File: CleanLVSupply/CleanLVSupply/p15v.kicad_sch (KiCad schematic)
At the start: 19 parts, among them U3 LMR64010XMF, U4 TPS7A47

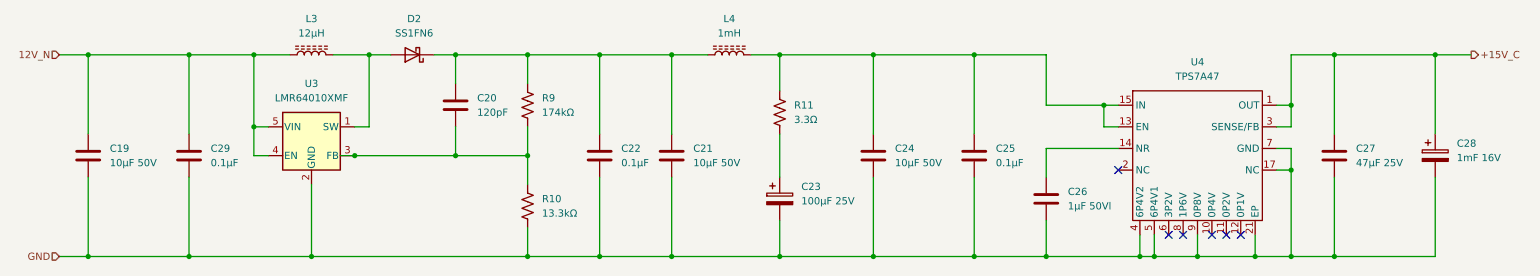
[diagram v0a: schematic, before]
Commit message: CleanLVSupply routing progress
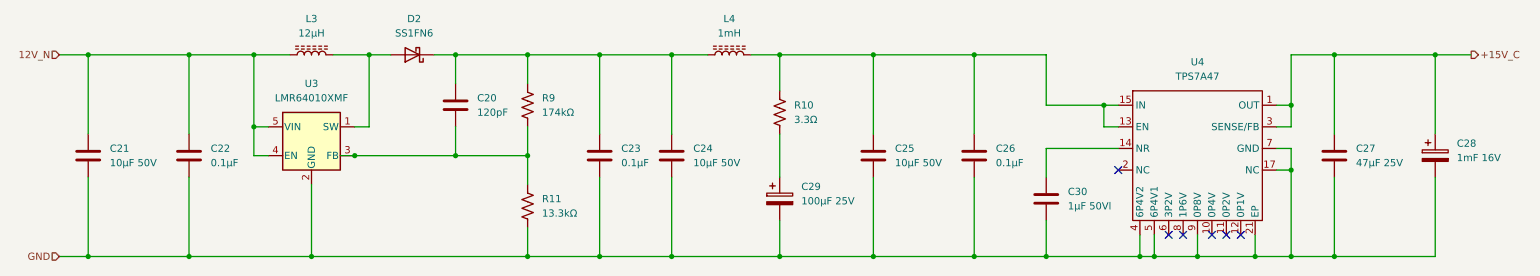
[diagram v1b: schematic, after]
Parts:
- renumbered C19 to C21, C29 to C22, C22 to C23, C21 to C24, C24 to C25, C25 to C26, C23 to C29, C26 to C30, R11 to R10, R10 to R11
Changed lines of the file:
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@@
 		(dnp no)
 		(fields_autoplaced yes)
-		(property "Reference" "C21"
+		(property "Reference" "C24"
 			(at 137.16 102.8699 0)
 			(effects
@@
 			(project "CleanLVSupply"
 				(path "/4327ef59-ef76-48f2-90b1-1a9e4399cfc2/f3bbc2e7-9beb-4b47-822a-03b189fc8c9b"
-					(reference "C21")
+					(reference "C24")
 					(unit 1)
 				)
@@
 		(dnp no)
 		(fields_autoplaced yes)
-		(property "Reference" "C24"
+		(property "Reference" "C25"
 			(at 172.72 102.8699 0)
 			(effects
@@
 			(project "CleanLVSupply"
 				(path "/4327ef59-ef76-48f2-90b1-1a9e4399cfc2/f3bbc2e7-9beb-4b47-822a-03b189fc8c9b"
-					(reference "C24")
+					(reference "C25")
 					(unit 1)
 				)
@@
 		(dnp no)
 		(fields_autoplaced yes)
-		(property "Reference" "C23"
+		(property "Reference" "C29"
 			(at 156.21 109.6009 0)
 			(effects
@@
 			(project "CleanLVSupply"
 				(path "/4327ef59-ef76-48f2-90b1-1a9e4399cfc2/f3bbc2e7-9beb-4b47-822a-03b189fc8c9b"
-					(reference "C23")
+					(reference "C29")
 					(unit 1)
 				)
@@
 		(dnp no)
 		(fields_autoplaced yes)
-		(property "Reference" "R10"
+		(property "Reference" "R11"
 			(at 110.49 111.7599 0)
 			(effects
@@
 			(project "CleanLVSupply"
 				(path "/4327ef59-ef76-48f2-90b1-1a9e4399cfc2/f3bbc2e7-9beb-4b47-822a-03b189fc8c9b"
-					(reference "R10")
+					(reference "R11")
 					(unit 1)
 				)
@@
 		(dnp no)
 		(fields_autoplaced yes)
-		(property "Reference" "C25"
+		(property "Reference" "C26"
 			(at 190.5 102.8699 0)
 			(effects
@@
 			(project "CleanLVSupply"
 				(path "/4327ef59-ef76-48f2-90b1-1a9e4399cfc2/f3bbc2e7-9beb-4b47-822a-03b189fc8c9b"
-					(reference "C25")
+					(reference "C26")
 					(unit 1)
 				)
@@
 		(dnp no)
 		(fields_autoplaced yes)
-		(property "Reference" "C26"
+		(property "Reference" "C30"
 			(at 203.2 110.4899 0)
 			(effects
@@
 			(project "CleanLVSupply"
 				(path "/4327ef59-ef76-48f2-90b1-1a9e4399cfc2/f3bbc2e7-9beb-4b47-822a-03b189fc8c9b"
-					(reference "C26")
+					(reference "C30")
 					(unit 1)
 				)
@@
 		(dnp no)
 		(fields_autoplaced yes)
-		(property "Reference" "R11"
+		(property "Reference" "R10"
 			(at 154.94 95.2499 0)
 			(effects
@@
 			(project "CleanLVSupply"
 				(path "/4327ef59-ef76-48f2-90b1-1a9e4399cfc2/f3bbc2e7-9beb-4b47-822a-03b189fc8c9b"
-					(reference "R11")
+					(reference "R10")
 					(unit 1)
 				)
@@
 		(dnp no)
 		(fields_autoplaced yes)
-		(property "Reference" "C22"
+		(property "Reference" "C23"
 			(at 124.46 102.8699 0)
 			(effects
@@
 			(project "CleanLVSupply"
 				(path "/4327ef59-ef76-48f2-90b1-1a9e4399cfc2/f3bbc2e7-9beb-4b47-822a-03b189fc8c9b"
-					(reference "C22")
+					(reference "C23")
 					(unit 1)
 				)
@@
 		(dnp no)
 		(fields_autoplaced yes)
-		(property "Reference" "C19"
+		(property "Reference" "C21"
 			(at 34.29 102.8699 0)
 			(effects
@@
 			(project "CleanLVSupply"
 				(path "/4327ef59-ef76-48f2-90b1-1a9e4399cfc2/f3bbc2e7-9beb-4b47-822a-03b189fc8c9b"
-					(reference "C19")
+					(reference "C21")
 					(unit 1)
 				)
@@
 		(dnp no)
 		(fields_autoplaced yes)
-		(property "Reference" "C29"
+		(property "Reference" "C22"
 			(at 52.07 102.8699 0)
 			(effects
@@
 			(project "CleanLVSupply"
 				(path "/4327ef59-ef76-48f2-90b1-1a9e4399cfc2/f3bbc2e7-9beb-4b47-822a-03b189fc8c9b"
-					(reference "C29")
-					(unit 1)
-				)
+					(reference "C22")
+					(unit 1)
+				)
